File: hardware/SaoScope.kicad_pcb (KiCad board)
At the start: 2 copper layers, 50 x 64 mm, 37 parts, among them J1 Conn_01x03_Pin, J2 Conn_01x04_Socket, SW1 TS-1077S-AR02016, SW2 TS-1077S-AR02016, SW3 TS-1077S-AR02016, SW4 TS-1077S-AR02016, SW5 TS-1077S-AR02016, U1 STM32G030F6Px, U2 LMC7660, U3 OPA197xDBV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

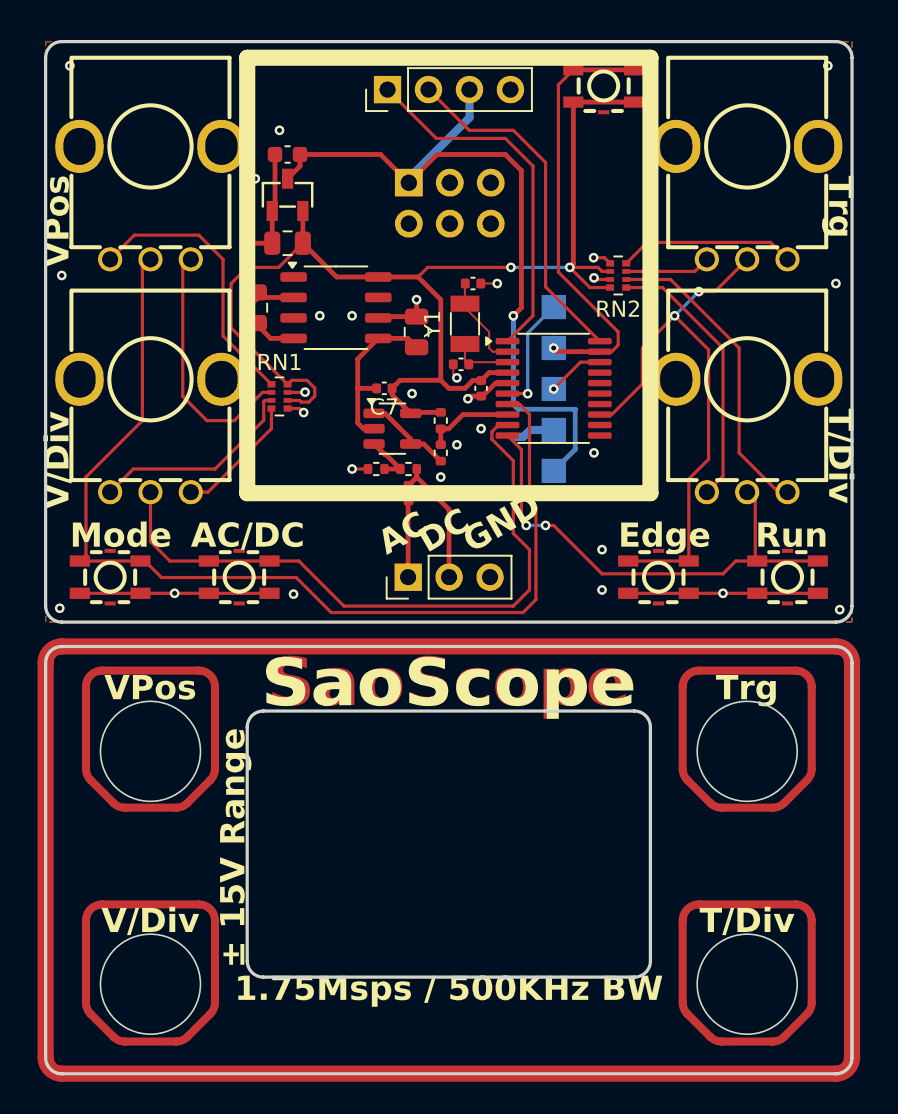
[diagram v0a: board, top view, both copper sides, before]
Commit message: split faceplate to another file
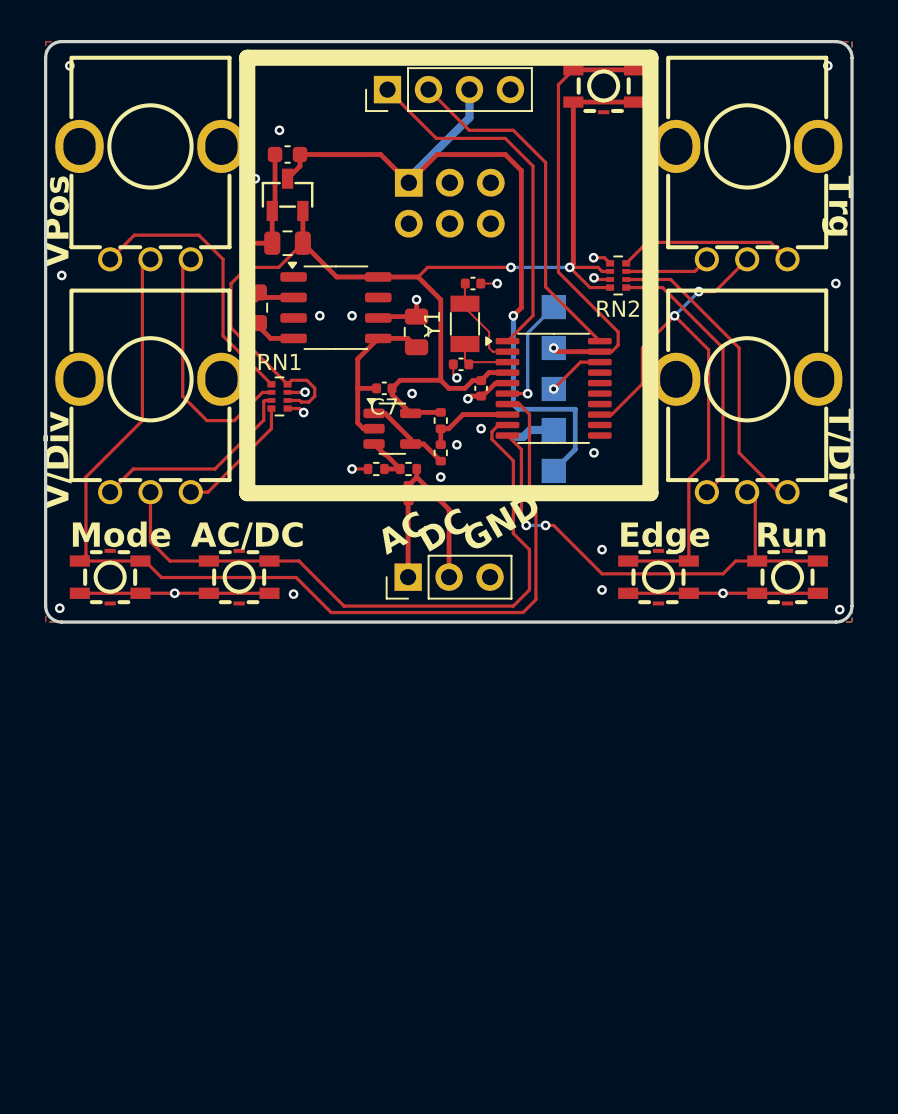
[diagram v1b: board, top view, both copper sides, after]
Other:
- board size 50 x 64 mm -> 50 x 36 mm
- board text removed: "1.75Msps / 500KHz BW"
- board text removed: "± 15V Range"

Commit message: switch 800k with two 1.6M resistors
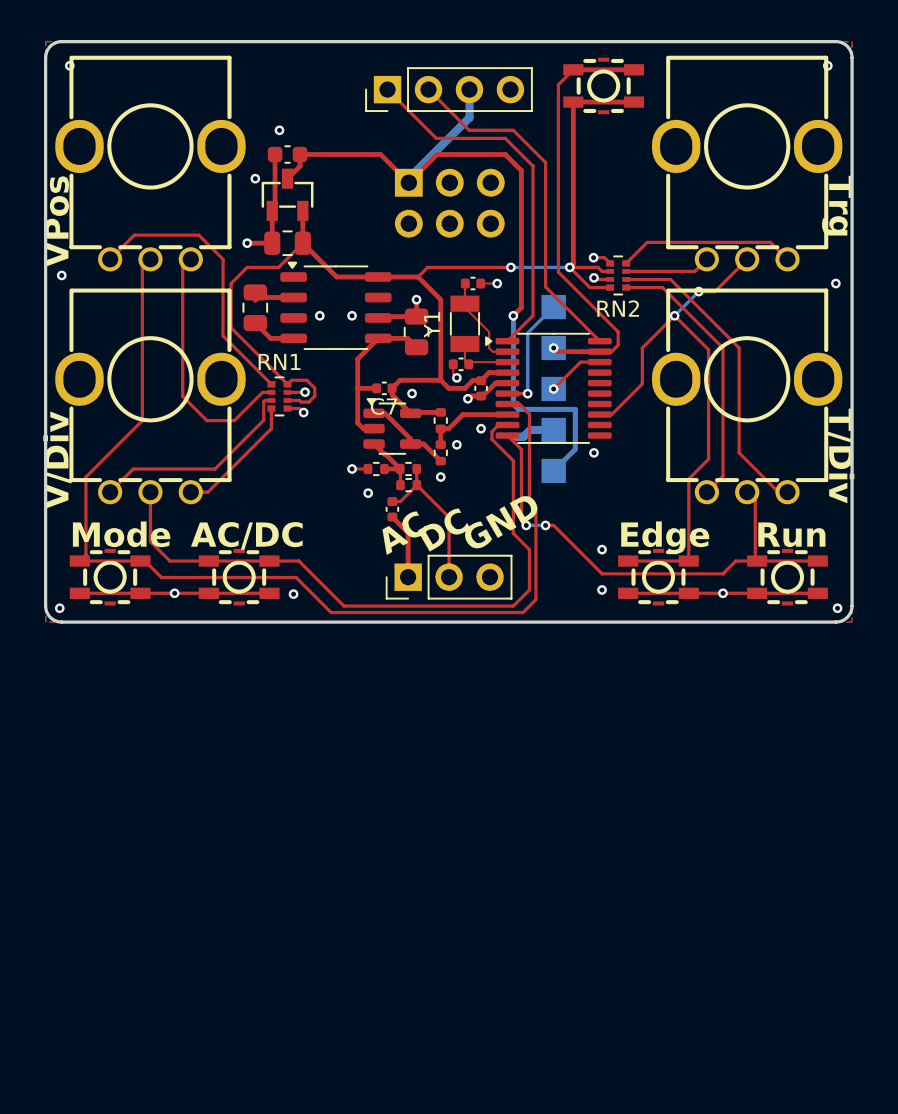
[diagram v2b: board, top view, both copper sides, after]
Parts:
- added R9: 1.6M 1%, Resistor_SMD:R_0402_1005Metric, F.Cu at (115.5, 88.5)
- R1: value 800K 1% -> 1.6M 1%
- moved C4 1.41 mm to (114.5, 90.0)
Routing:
- net Net-(J1-Pin_2): track 8.26 -> 9.48 mm
- net Net-(U3-+): track 3.25 -> 4.25 mm
- net Net-(J1-Pin_1): track 4.70 -> 4.13 mm

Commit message: bring in i2c lines from sao, a gpio, and run a sig gen line out. rework button labels.
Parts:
- removed SW5: TS-1077S-AR02016, easyeda2kicad:KEY-SMD_4P-L3.1-W3.1-P2.00-LS4.0
- added C10: 1pF, Capacitor_SMD:C_0402_1005Metric, F.Cu at (115.5, 89.5)
- added R10: 47, Resistor_SMD:R_0402_1005Metric, F.Cu at (117.0, 88.8)
- added R11: 100, Resistor_SMD:R_0402_1005Metric, F.Cu at (129.0, 84.0)
- C4: value .1uF -> 1uF; footprint Capacitor_SMD:C_0402_1005Metric -> Capacitor_SMD:C_0603_1608Metric
- J1: value Conn_01x03_Pin -> Conn_01x04_Pin; footprint Connector_PinHeader_2.54mm:PinHeader_1x03_P2.54mm_Vertical -> Connector_PinHeader_2.54mm:PinHeader_1x04_P2.54mm_Vertical
- moved J2 7.80 mm to (122.0, 64.0), turned to -90 degrees
- moved C4 1.99 mm to (112.5, 90.2), turned to 180 degrees
- moved J1 1.28 mm to (114.2, 94.2)
- moved RN2 0.75 mm to (129.2, 75.5)
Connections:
- U1 pad 14: /I2S1_SD -> /SIGGEN
- U1 pad 16: /PA11/PA9 -> /I2C2_SCL
- U1 pad 17: /PA12/PA10 -> /I2C2_SDA
- X1 pad 3: unconnected-(X1-SDA-Pad3) -> /I2C2_SDA
- X1 pad 4: unconnected-(X1-SCL-Pad4) -> /I2C2_SCL
- X1 pad 5: unconnected-(X1-GPIO1-Pad5) -> /PA4
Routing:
- net /SYS_SWCLK: track 27.0 -> 2.96 mm
- net /I2C2_SDA: track 0.00 -> 22.3 mm, vias 0 -> 1
- net /PA4: track 0.00 -> 21.1 mm, vias 0 -> 3
- net /I2C2_SCL: track 0.00 -> 20.0 mm, vias 0 -> 1
- net Net-(J1-Pin_4): track 0.00 -> 14.4 mm, vias 0 -> 1
- net +3V0: track 75.8 -> 62.6 mm
- net /I2C1_SDA: track 22.5 -> 17.0 mm, vias 0 -> 1
- net Net-(J1-Pin_2): track 9.48 -> 13.0 mm
- net /I2C1_SCL: track 21.6 -> 18.9 mm
- net /SIGGEN: track 0.00 -> 1.64 mm
- net /DIAL3: track 30.2 -> 31.5 mm
- net Net-(C10-Pad2): track 0.00 -> 1.14 mm
- net Net-(U3-+): track 4.25 -> 5.25 mm
- net +3.3V: track 47.8 -> 46.8 mm
- net Net-(J1-Pin_1): track 4.13 -> 5.01 mm
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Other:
- board text added: "2024 Ben Hencke"
- board text added: "EDGE"
- board text added: "RUN"
- board text added: "SIG"
- board text added: "± 15V Range"
- board text removed: "AC/DC"
- board text removed: "Edge"
- board text removed: "Run"
